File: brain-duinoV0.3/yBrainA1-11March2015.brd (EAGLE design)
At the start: 81.4 x 53.3 mm, 137 parts, among them IC1 OP2177ARMZ, IC2 OPA2111KP, IC3 OP4177ARZ, IC4 OPA2111KP, IC5 TLC555CDR, IC6 TAR5SB50, IC7 LT1761ES5-5, K1 AQY221R2VY, K2 AQY221R2VY

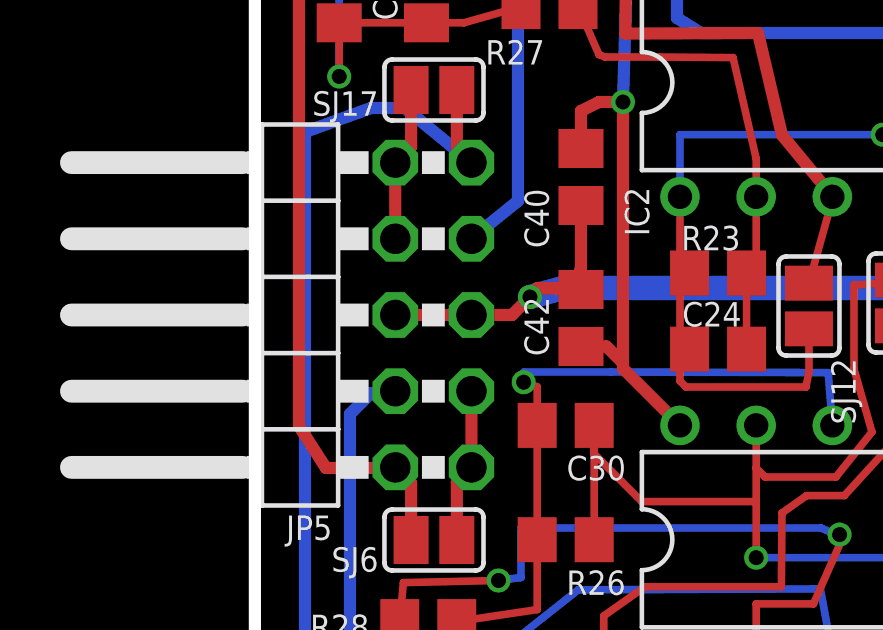
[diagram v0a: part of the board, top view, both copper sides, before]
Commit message: added values to devices where ERC requires it.
Signed-off-by: Christoph Maier <cm.hardware.software.elsewhere@gmail.com>
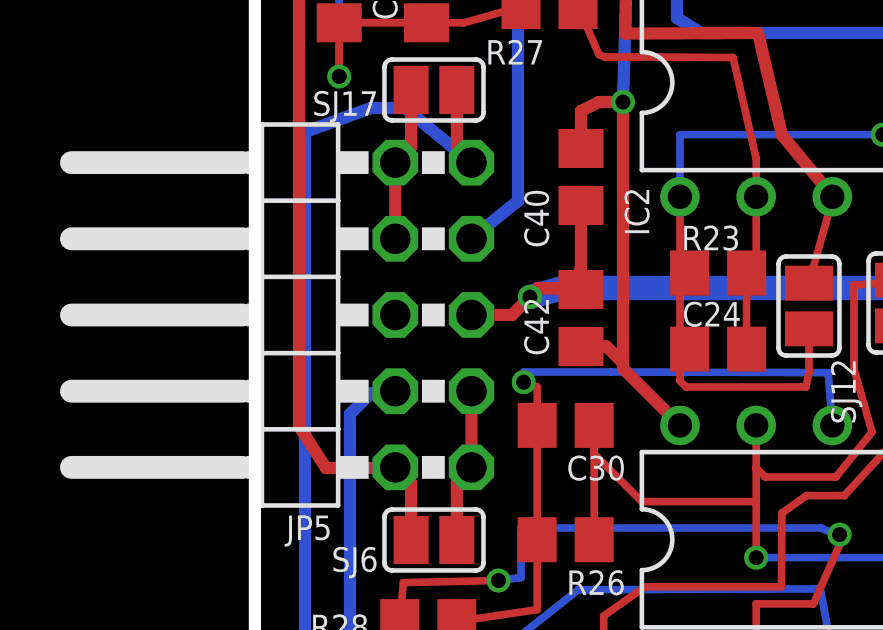
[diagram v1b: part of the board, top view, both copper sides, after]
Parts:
- AD, GND, ICSP, IOH, IOL, JP5, POWER, RXD, SJ1, SJ10, SJ11, SJ12, SJ13, SJ14, SJ15, SJ16, SJ17, SJ2, SJ3, SJ4, SJ5, SJ6, SJ7, SJ8, SJ9, TXD, VCC: value (none) -> .
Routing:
- net GND: track 494.7 -> 492.2 mm
